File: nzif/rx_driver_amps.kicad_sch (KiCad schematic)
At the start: 84 parts, among them U117 LT5400BCMS8E-8-TRPBF, U118 LT5400BCMS8E-8-TRPBF, U119 ADG884xCP, U120 ADG884xCP, U121 ADA4945-1, U122 ADA4945-1, U123 LT5400BCMS8E-8-TRPBF, U124 LT5400BCMS8E-8-TRPBF, U125 ADG884xCP, U126 ADG884xCP, U127 ADA4945-1, U128 ADA4945-1

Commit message: Digikey parts for rcv stages
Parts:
- C109, C110, C115, C116, C127, C130, C133, C136, C212, C213, C215, C221: Digikey Part # (none) -> 587-3258-1-ND
- C111, C112, C113, C114, C117, C118, C119, C120, C121, C122, C128, C129, C131, C132, C134, C135, C137, C138, C139, C142, C211, C214, C216, C222: Digikey Part # (none) -> 490-GCM31C5C1H104FA16LCT-ND
- C123, C124, C125, C126, C140, C141, C143, C144: footprint (none) -> Resistor_SMD:R_0603_1608Metric_Pad0.98x0.95mm_HandSolder; Digikey Part # (none) -> 490-GCM31C5C1H104FA16LCT-ND
- R104, R106, R118, R122: Digikey Part # (none) -> 311-3.40KHRCT-ND
- R105, R107, R115, R117, R119, R123, R129, R131: Digikey Part # (none) -> 311-9.53KHRCT-ND
- R108, R109, R110, R111, R120, R121, R125, R126: footprint (none) -> Resistor_SMD:R_0603_1608Metric_Pad0.98x0.95mm_HandSolder; Digikey Part # (none) -> 311-1.00KHRCT-ND
- R112, R113, R114, R116, R124, R127, R128, R130: Digikey Part # (none) -> 311-10.0KHRCT-ND
- U117, U118, U123, U124: Digikey Part # (none) -> LT5400BCMS8E-1#PBF-ND
- U119, U120, U125, U126: Digikey Part # (none) -> 505-ADG884BRMZ-ND

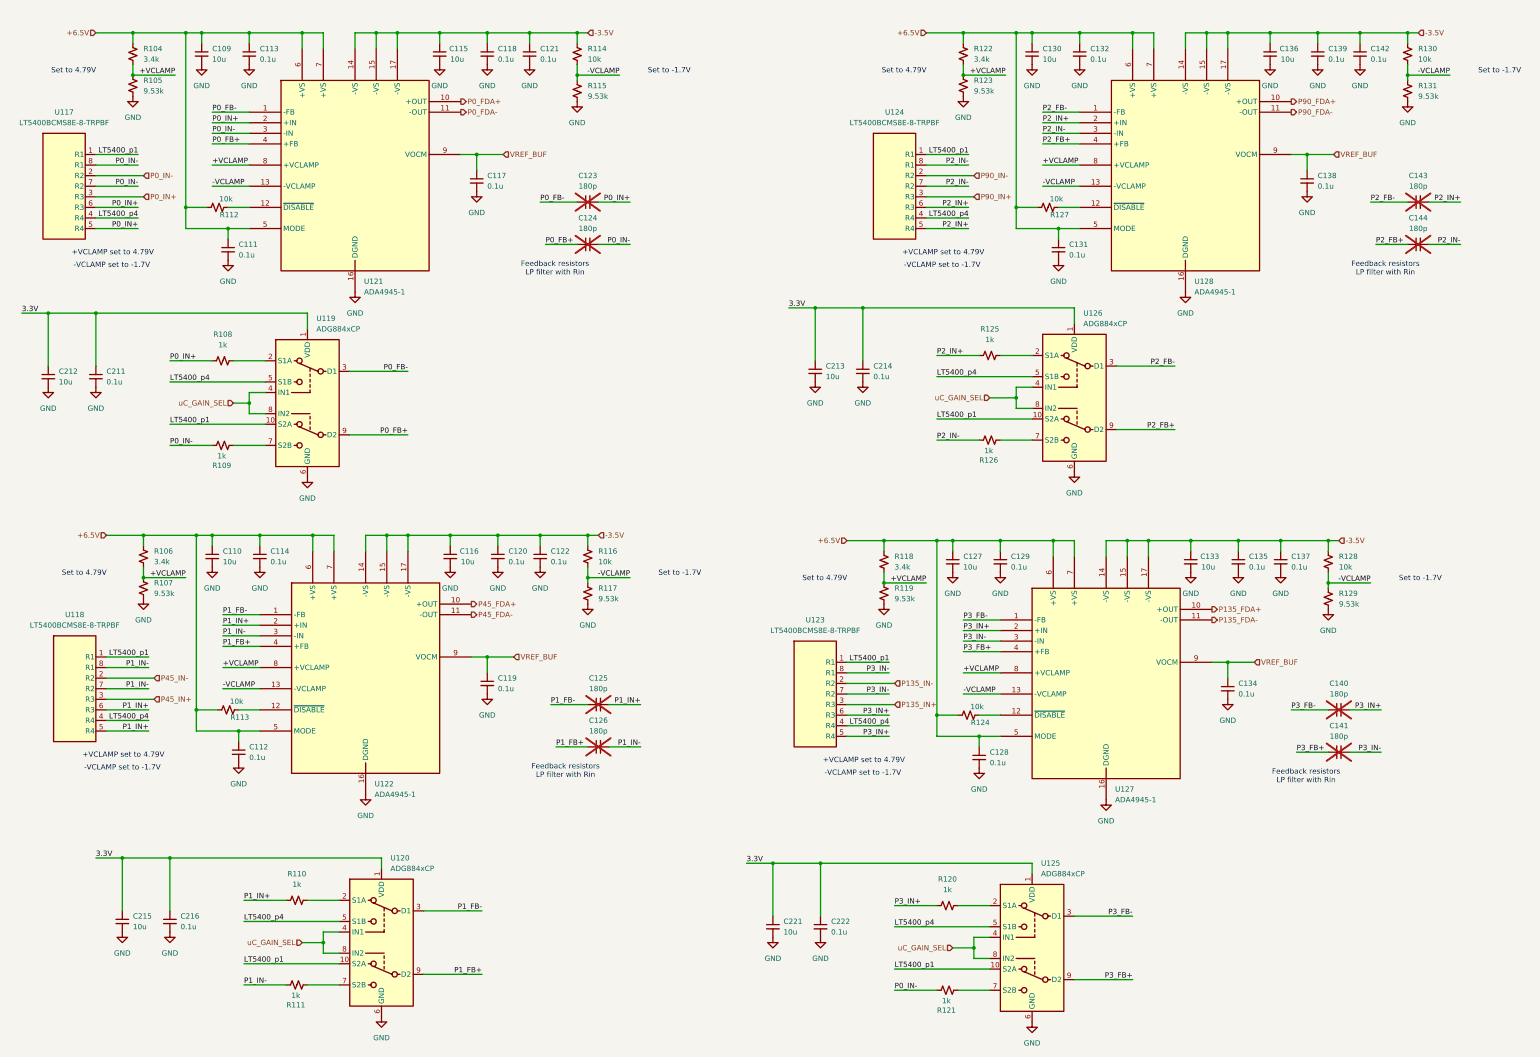
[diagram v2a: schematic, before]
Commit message: add annotations - first run of erc
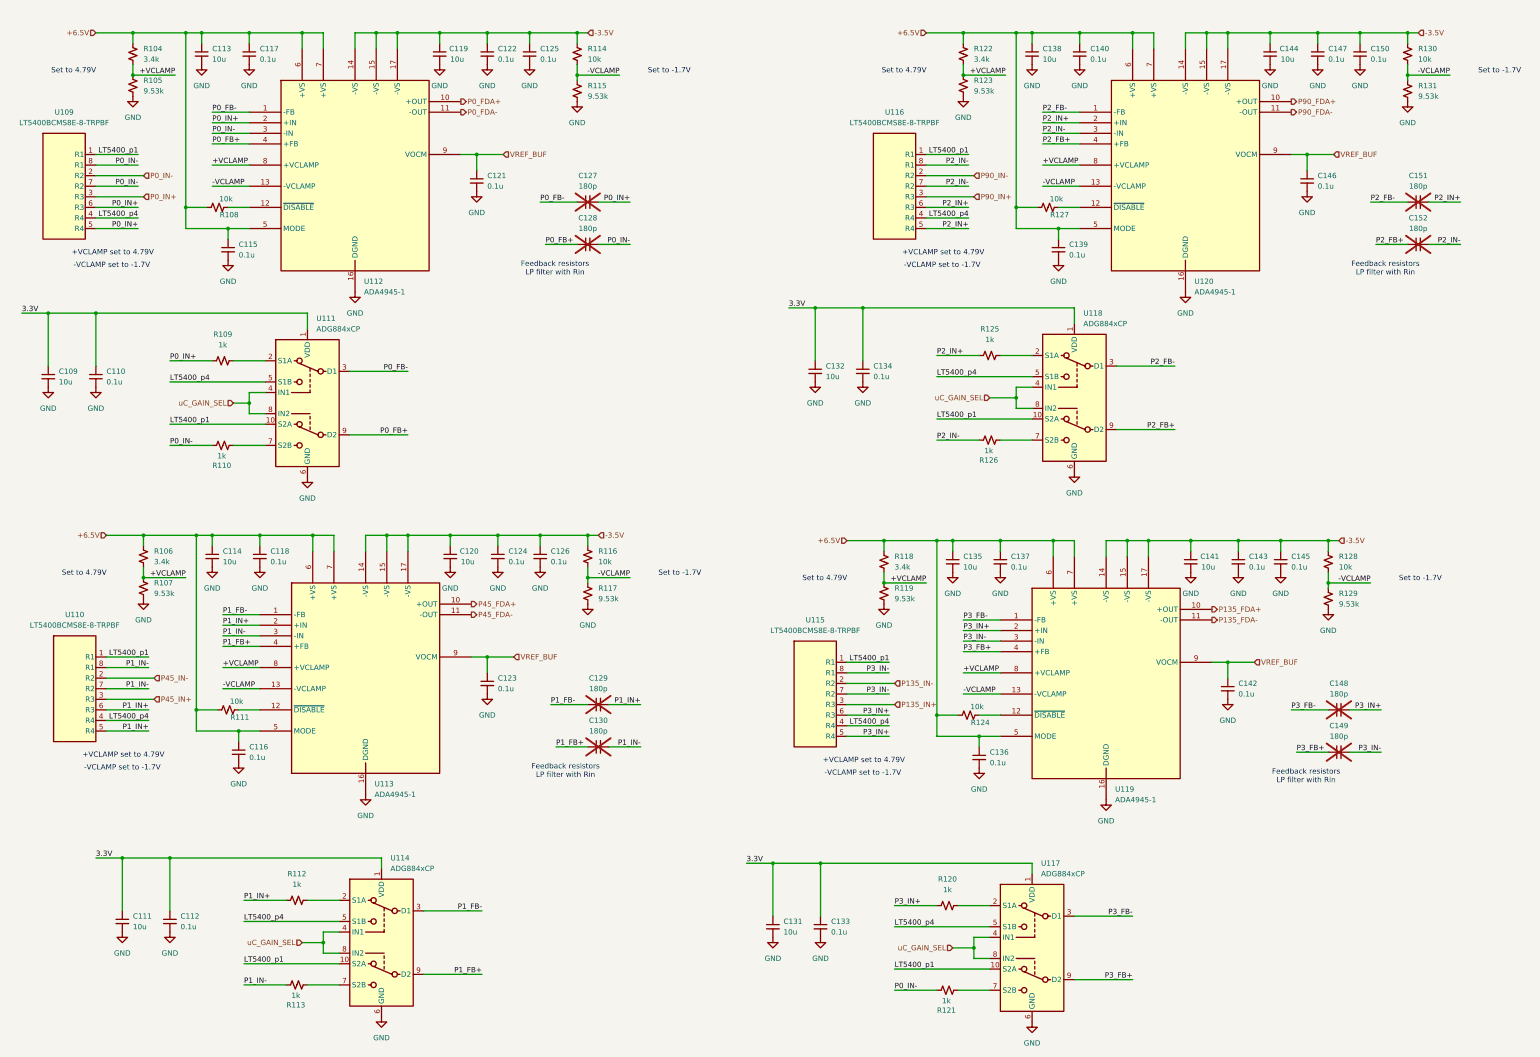
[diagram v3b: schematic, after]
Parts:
- renumbered C212 to C109, C211 to C110, C215 to C111, C216 to C112, C109 to C113, C110 to C114, C111 to C115, C112 to C116, C113 to C117, C114 to C118, C115 to C119, C116 to C120, C117 to C121, C118 to C122, C119 to C123, C120 to C124, C121 to C125, C122 to C126, C123 to C127, C124 to C128, C125 to C129, C126 to C130, C221 to C131, C213 to C132, C222 to C133, C214 to C134, C127 to C135, C128 to C136, C129 to C137, C130 to C138, C131 to C139, C132 to C140, C133 to C141, C134 to C142, C135 to C143, C136 to C144, C137 to C145, C138 to C146, C139 to C147, C140 to C148, C141 to C149, C142 to C150, C143 to C151, C144 to C152, R112 to R108, R108 to R109, R109 to R110, R113 to R111, R110 to R112, R111 to R113, U117 to U109, U118 to U110, U119 to U111, U121 to U112, U122 to U113, U120 to U114, U123 to U115, U124 to U116, U125 to U117, U126 to U118, U127 to U119, U128 to U120

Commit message: updated power on all schematics
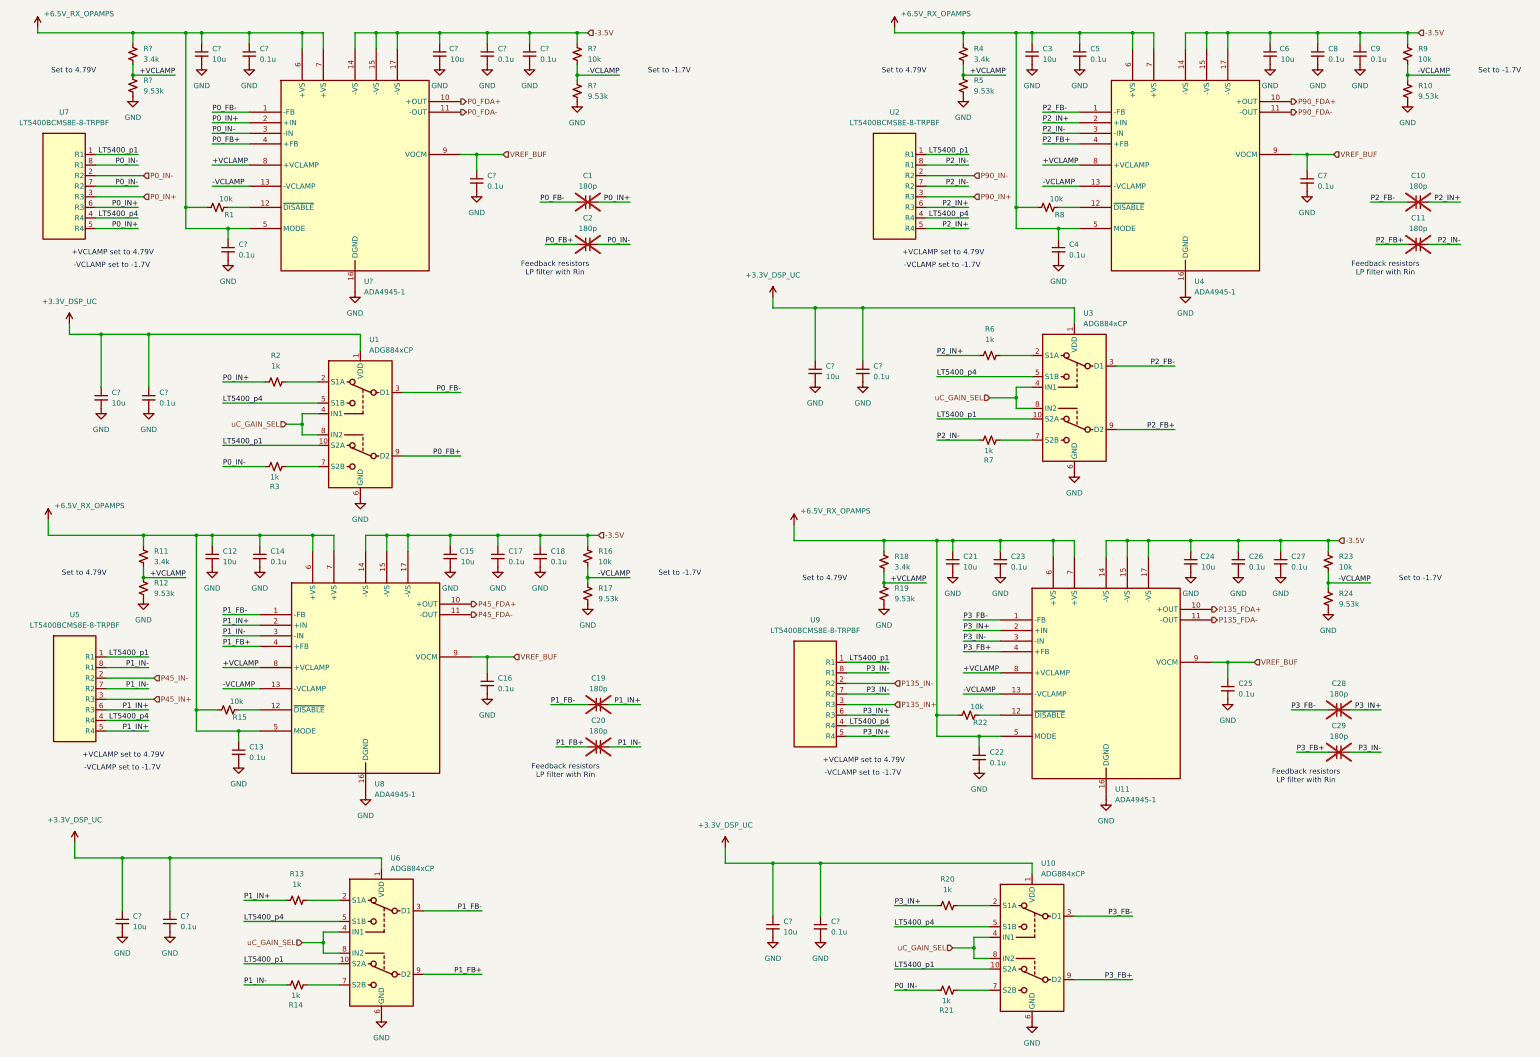
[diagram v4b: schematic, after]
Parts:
- renumbered C127 to C1, C151 to C10, C152 to C11, C114 to C12, C116 to C13, C118 to C14, C120 to C15, C123 to C16, C124 to C17, C126 to C18, C129 to C19, C128 to C2, C130 to C20, C135 to C21, C136 to C22, C137 to C23, C141 to C24, C142 to C25, C143 to C26, C145 to C27, C148 to C28, C149 to C29, C138 to C3, C139 to C4, C140 to C5, C144 to C6, C146 to C7, C147 to C8, C150 to C9, C113 to C?, C115 to C?, C131 to C?, C119 to C?, C121 to C?, C133 to C?, C111 to C?, C134 to C?, C117 to C?, C132 to C?, C110 to C?, C112 to C?, C125 to C?, C122 to C?, C109 to C?, R108 to R1, R131 to R10, R106 to R11, R107 to R12, R112 to R13, R113 to R14, R111 to R15, R116 to R16, R117 to R17, R118 to R18, R119 to R19, R109 to R2, R120 to R20, R121 to R21, R124 to R22, R128 to R23, R129 to R24, R110 to R3, R122 to R4, R123 to R5, R125 to R6, R126 to R7, R127 to R8, R130 to R9, R105 to R?, R104 to R?, R114 to R?, R115 to R?, U111 to U1, U117 to U10, U119 to U11, U116 to U2, U118 to U3, U120 to U4, U110 to U5, U114 to U6, U109 to U7, U113 to U8, U115 to U9, U112 to U?
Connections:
- net +6.5V renamed +6.5V_RX_OPAMPS
- net 3.3V renamed +3.3V_DSP_UC
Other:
- moved on the sheet: C?, R2, R3, U1

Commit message: cartoons on main2
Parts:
- gave numbers to parts that had none: 20
- renumbered C12 to C114, C13 to C116, C14 to C118, C15 to C120, C16 to C123, C17 to C124, C18 to C126, C1 to C127, C2 to C128, C19 to C129, C20 to C130, C21 to C135, C22 to C136, C23 to C137, C3 to C138, C4 to C139, C5 to C140, C24 to C141, C25 to C142, C26 to C143, C6 to C144, C27 to C145, C7 to C146, C8 to C147, C28 to C148, C29 to C149, C9 to C150, C10 to C151, C11 to C152, R11 to R106, R12 to R107, R1 to R108, R2 to R109, R3 to R110, R15 to R111, R13 to R112, R14 to R113, R16 to R116, R17 to R117, R18 to R118, R19 to R119, R20 to R120, R21 to R121, R4 to R122, R5 to R123, R22 to R124, R6 to R125, R7 to R126, R8 to R127, R23 to R128, R24 to R129, R9 to R130, R10 to R131, U7 to U109, U5 to U110, U1 to U111, U8 to U113, U6 to U114, U9 to U115, U2 to U116, U10 to U117, U3 to U118, U11 to U119, U4 to U120

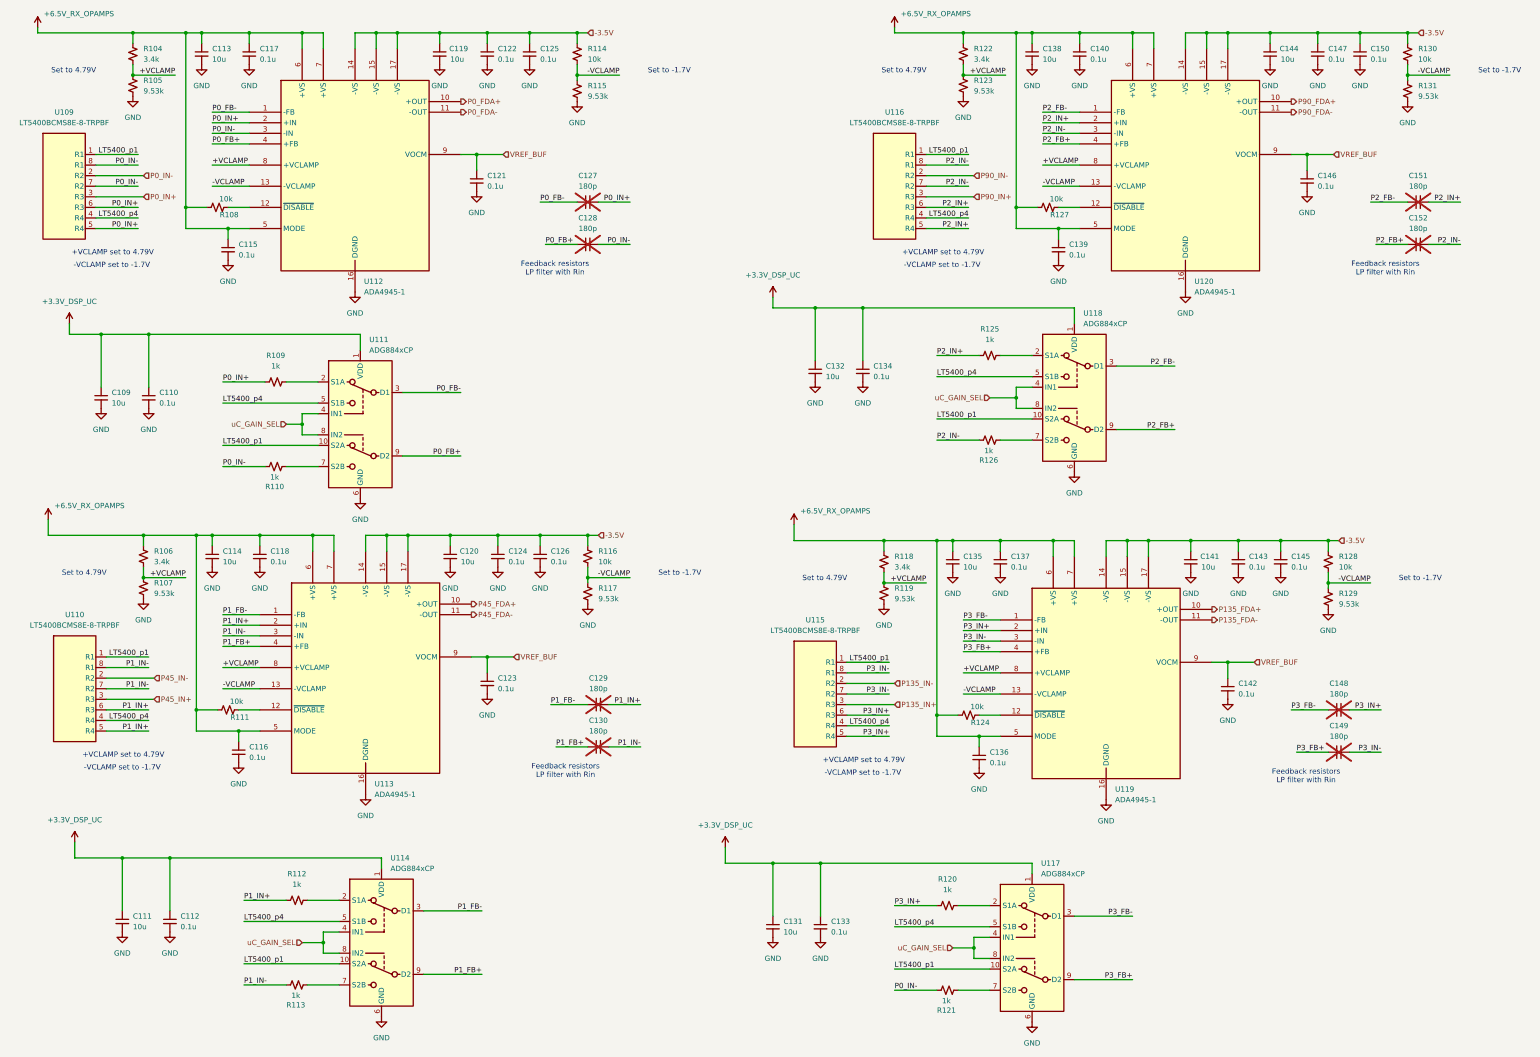
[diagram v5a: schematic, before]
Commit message: wire top sheet from rf front end through rx driver amps
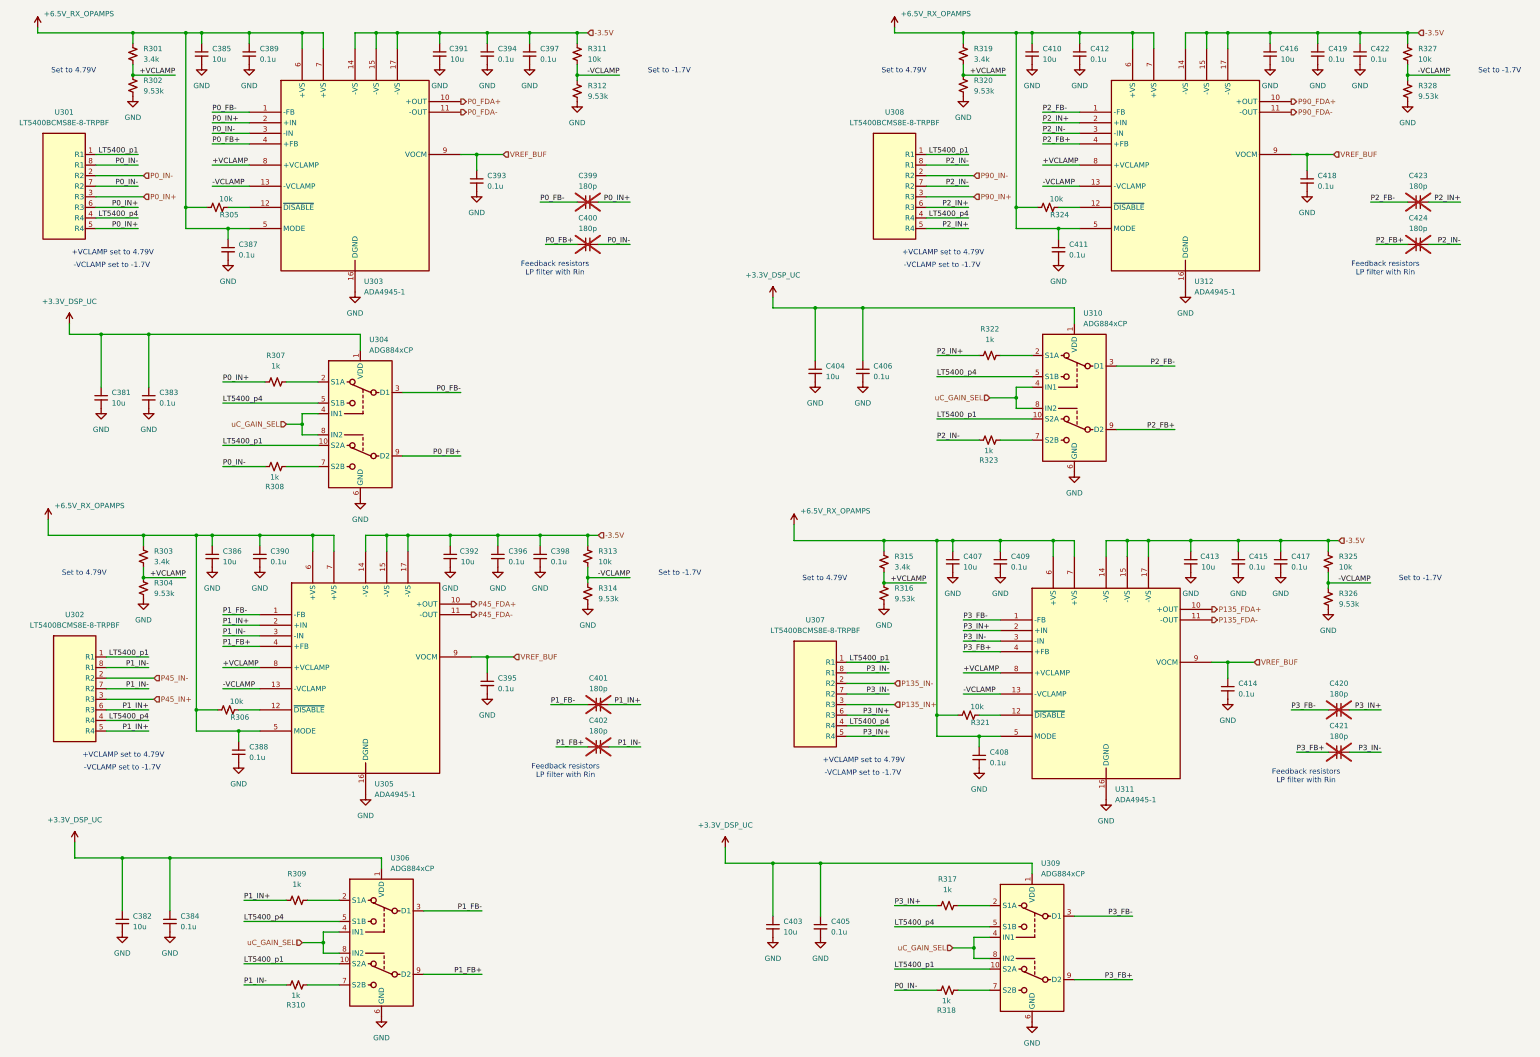
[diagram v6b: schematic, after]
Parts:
- renumbered C109 to C381, C111 to C382, C110 to C383, C112 to C384, C113 to C385, C114 to C386, C115 to C387, C116 to C388, C117 to C389, C118 to C390, C119 to C391, C120 to C392, C121 to C393, C122 to C394, C123 to C395, C124 to C396, C125 to C397, C126 to C398, C127 to C399, C128 to C400, C129 to C401, C130 to C402, C131 to C403, C132 to C404, C133 to C405, C134 to C406, C135 to C407, C136 to C408, C137 to C409, C138 to C410, C139 to C411, C140 to C412, C141 to C413, C142 to C414, C143 to C415, C144 to C416, C145 to C417, C146 to C418, C147 to C419, C148 to C420, C149 to C421, C150 to C422, C151 to C423, C152 to C424, R104 to R301, R105 to R302, R106 to R303, R107 to R304, R108 to R305, R111 to R306, R109 to R307, R110 to R308, R112 to R309, R113 to R310, R114 to R311, R115 to R312, R116 to R313, R117 to R314, R118 to R315, R119 to R316, R120 to R317, R121 to R318, R122 to R319, R123 to R320, R124 to R321, R125 to R322, R126 to R323, R127 to R324, R128 to R325, R129 to R326, R130 to R327, R131 to R328, U109 to U301, U110 to U302, U112 to U303, U111 to U304, U113 to U305, U114 to U306, U115 to U307, U116 to U308, U117 to U309, U118 to U310, U119 to U311, U120 to U312
